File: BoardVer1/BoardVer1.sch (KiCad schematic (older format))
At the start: 78 parts, among them J1 Vin, J2 Motor conn, J3 FTDI_basic, J4 LED strip, J5 Swiss Sonic cable, J6 CycleStartBtn, J7 MicroSwitches, J8 Estop, J9 SonicGND, SW1 SW_Push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

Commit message: First layout complete
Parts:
- removed C1, C2: 100uF, Capacitor_SMD:C_0805_2012Metric_Pad1.15x1.40mm_HandSolder, symbol Device:CP
- removed C12, C13: 15p, Capacitor_SMD:C_0805_2012Metric_Pad1.15x1.40mm_HandSolder, symbol Device:C_Small
- removed C3: 10n, Capacitor_SMD:C_0805_2012Metric_Pad1.15x1.40mm_HandSolder, symbol Device:C_Small
- removed C8, C9: 100n, Capacitor_SMD:C_0805_2012Metric_Pad1.15x1.40mm_HandSolder, symbol Device:C_Small
- removed D3: D_Schottky, Diode_SMD:D_SMB_Handsoldering, symbol Device:D_Schottky
- removed J3: FTDI_basic, Connector_PinHeader_2.54mm:PinHeader_1x06_P2.54mm_Vertical, symbol Connector:Conn_01x06_Male
- removed L1: 47uH, Inductor_SMD:L_Neosid_SM-NE127_HandSoldering, symbol Device:L
- removed R2: 1K, Resistor_SMD:R_0805_2012Metric_Pad1.15x1.40mm_HandSolder, symbol Device:R_Small
- removed R3: 3K, Resistor_SMD:R_0805_2012Metric_Pad1.15x1.40mm_HandSolder, symbol Device:R_Small
- removed R4: 10K, Resistor_SMD:R_0805_2012Metric_Pad1.15x1.40mm_HandSolder, symbol Device:R_Small
- removed SW1: SW_Push, Button_Switch_SMD:SW_SPST_B3S-1000, symbol Switch:SW_Push
- removed U2: LM2675M-ADJ, Package_SO:SOIC-8_3.9x4.9mm_P1.27mm, symbol Regulator_Switching:LM2675M-ADJ
- removed U3: ATMEGA328PB-AU_Arduino, Package_QFP:TQFP-32_7x7mm_P0.8mm, symbol Peters:ATMEGA328PB-AU_Arduino
- removed Y1: 16MHZ, Crystal:Crystal_HC49-4H_Vertical, symbol Device:Crystal
- added A1: Arduino_Nano_v3.x, Module:Arduino_Nano, symbol MCU_Module:Arduino_Nano_v3.x
- added C2: 10uF/50V, Capacitor_SMD:C_2010_5025Metric_Pad1.52x2.65mm_HandSolder, symbol Device:C
- added C3: 22uF/16V, Capacitor_SMD:C_2010_5025Metric_Pad1.52x2.65mm_HandSolder, symbol Device:C
- added U2: V7805-1000, digikey-footprints:3-SIP_Module_V7805-1000, symbol dk_DC-DC-Converters:V7805-1000
- F1, F2: footprint Fuse:Fuse_1210_3225Metric_Pad1.42x2.65mm_HandSolder -> Fuse:Fuse_2010_5025Metric_Pad1.52x2.65mm_HandSolder
- J1: footprint TerminalBlock_4Ucon:TerminalBlock_4Ucon_1x02_P3.50mm_Horizontal -> TerminalBlock:TerminalBlock_bornier-2_P5.08mm
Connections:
- net labels removed: DTR, RXI, TXO
- wire segments 213 -> 187
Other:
- note removed: "Feedback voltage devider:\nVout=1.23(1+3000/1000) = 4,92Volt\nVout=1.23(1+1540/910) = 3,31Volt"
- moved on the sheet: C10, C14, C4, D1, D2, D4, D5, F1, J1, R1, R5, R6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

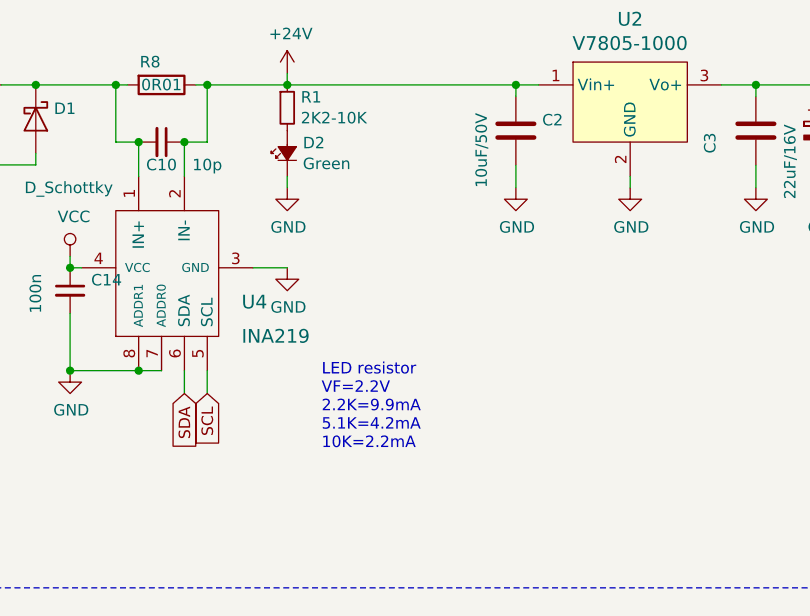
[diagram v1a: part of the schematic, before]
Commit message: Less vias
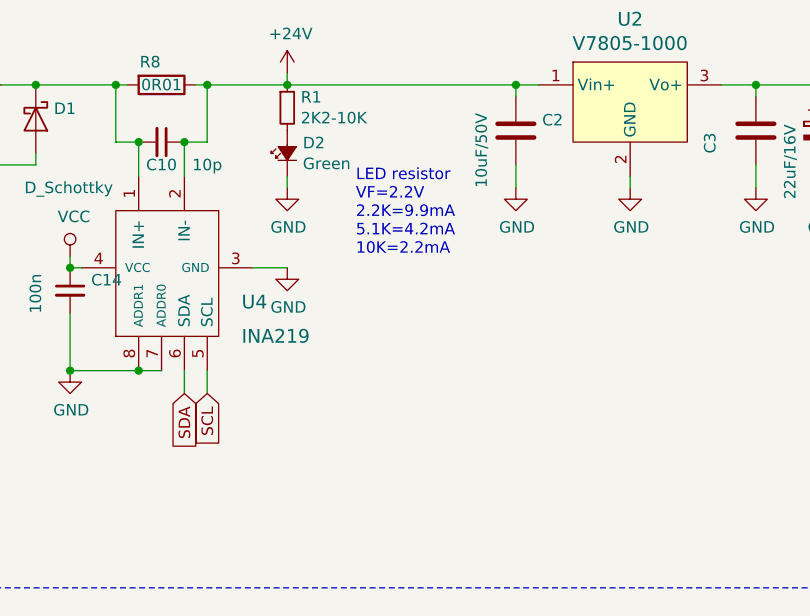
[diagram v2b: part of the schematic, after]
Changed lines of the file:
@@
 Wire Wire Line
 	3700 2350 3350 2350
-Text Notes 3850 3950 0    50   ~ 0
+Text Notes 4000 3100 0    50   ~ 0
 LED resistor\nVF=2.2V\n2.2K=9.9mA\n5.1K=4.2mA\n10K=2.2mA
 Text GLabel 2400 8350 0    50   Input ~ 0

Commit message: Better layout
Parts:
- removed J2: Motor conn, TerminalBlock_4Ucon:TerminalBlock_4Ucon_1x04_P3.50mm_Horizontal, symbol Connector:Screw_Terminal_01x04
- removed J6: CycleStartBtn, TerminalBlock:TerminalBlock_bornier-2_P5.08mm, symbol Connector:Screw_Terminal_01x02
- removed J7: MicroSwitches, TerminalBlock:TerminalBlock_bornier-6_P5.08mm, symbol Connector:Screw_Terminal_01x06
- removed R21: 10K, Resistor_SMD:R_0805_2012Metric_Pad1.15x1.40mm_HandSolder, symbol Device:R_Small
- removed RLY1: G5V-2-DC12, digikey-footprints:Relay_THT_G5V-2, symbol dk_Signal-Relays-Up-to-2-Amps:G5V-2-DC12
- added J2: Screw_Terminal_01x12, TerminalBlock_Phoenix:TerminalBlock_Phoenix_PT-1,5-12-3.5-H_1x12_P3.50mm_Horizontal, symbol Connector:Screw_Terminal_01x12
- added R2: 1K-2K, Resistor_SMD:R_0805_2012Metric_Pad1.15x1.40mm_HandSolder, symbol Device:R_Small
- added R3: 10K, Resistor_SMD:R_0805_2012Metric_Pad1.15x1.40mm_HandSolder, symbol Device:R_Small
- added R4: G6A-274P, Libs:OMRON_G6A-274P-ST, symbol Peters:G6A-274P
- added U3: PC817, Package_DIP:DIP-4_W7.62mm, symbol Isolator:PC817
- J9: footprint Connector_PinSocket_2.54mm:PinSocket_1x01_P2.54mm_Horizontal -> Connector_PinHeader_2.54mm:PinHeader_1x01_P2.54mm_Vertical
- U1: symbol TMC262_bob60V1-2:TMC262BOB -> BoardVer1-rescue:TMC262BOB-TMC262_bob60V1-2
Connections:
- net labels added: A1, A2, B1, B2, CycleStartBtn, DoorOpenBTN, PistonTop, PistonTopBTN, WindowShutBTN
- wire segments 187 -> 191
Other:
- note added: "Connectors"
- note removed: "LED strip"
- moved on the sheet: D7, F2, J4, J5, J8, J9, JP1, JP2, R11, R13, R20, U10

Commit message: BOM and polish
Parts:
- F1, F2: footprint Fuse:Fuse_2010_5025Metric_Pad1.52x2.65mm_HandSolder -> Libs:LittleFuse_110F_24V
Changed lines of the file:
@@
 F 0 "F1" V 2075 2350 50  0000 C CNN
 F 1 "Polyfuse" V 2166 2350 50  0000 C CNN
-F 2 "Fuse:Fuse_2010_5025Metric_Pad1.52x2.65mm_HandSolder" H 2350 2150 50  0001 L CNN
+F 2 "Libs:LittleFuse_110F_24V" H 2350 2150 50  0001 L CNN
 F 3 "~" H 2300 2350 50  0001 C CNN
 	1    2300 2350
@@
 F 0 "F2" V 10650 5500 50  0000 C CNN
 F 1 "100-300mA" V 10550 5500 50  0000 C CNN
-F 2 "Fuse:Fuse_2010_5025Metric_Pad1.52x2.65mm_HandSolder" H 10500 5300 50  0001 L CNN
+F 2 "Libs:LittleFuse_110F_24V" H 10500 5300 50  0001 L CNN
 F 3 "~" H 10450 5500 50  0001 C CNN
 	1    10450 5500
